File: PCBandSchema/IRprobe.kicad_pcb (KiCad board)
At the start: 2 copper layers, 24 x 16 mm, 21 parts, among them J1 Conn_01x03_Male, Q1 SFH3015FASMALL-FOOTPRINT, U1 ATtiny25-SSU

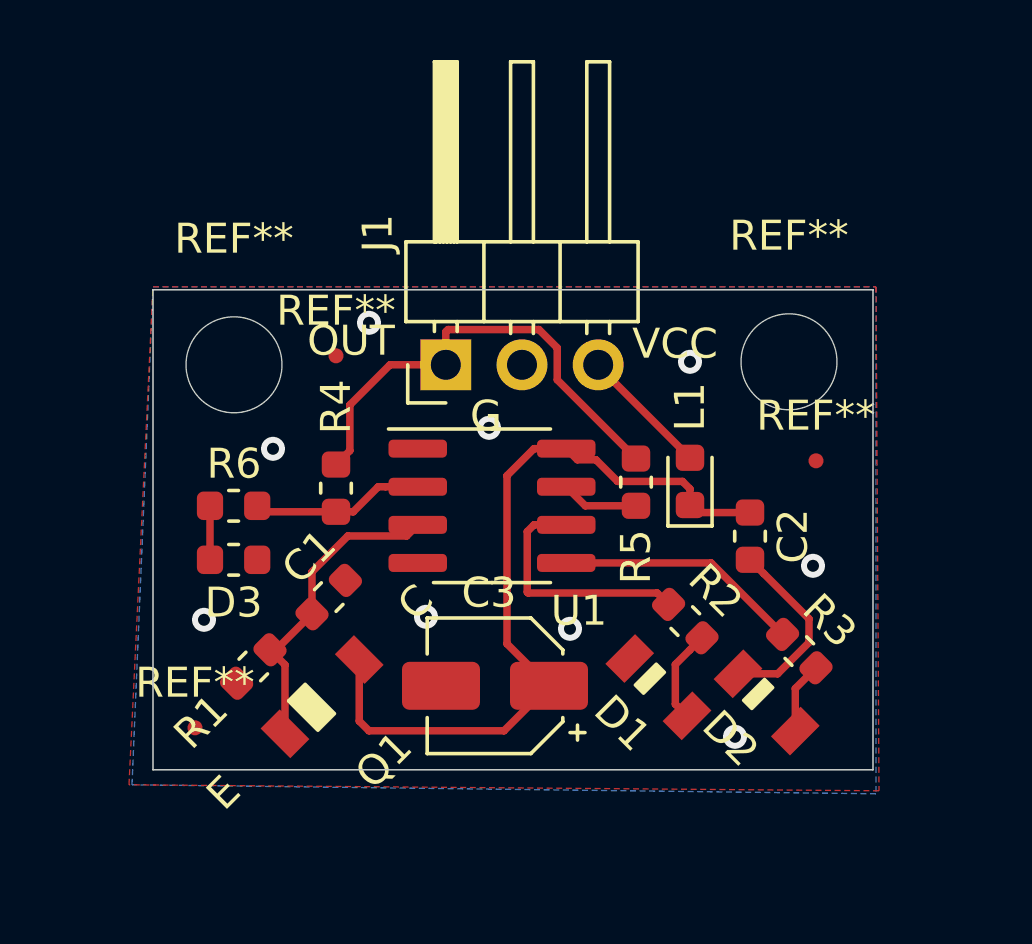
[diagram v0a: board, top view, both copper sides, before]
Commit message: Ver 2 Added ADXL
Second version with same footprint but added ADXL on top of IR probe.
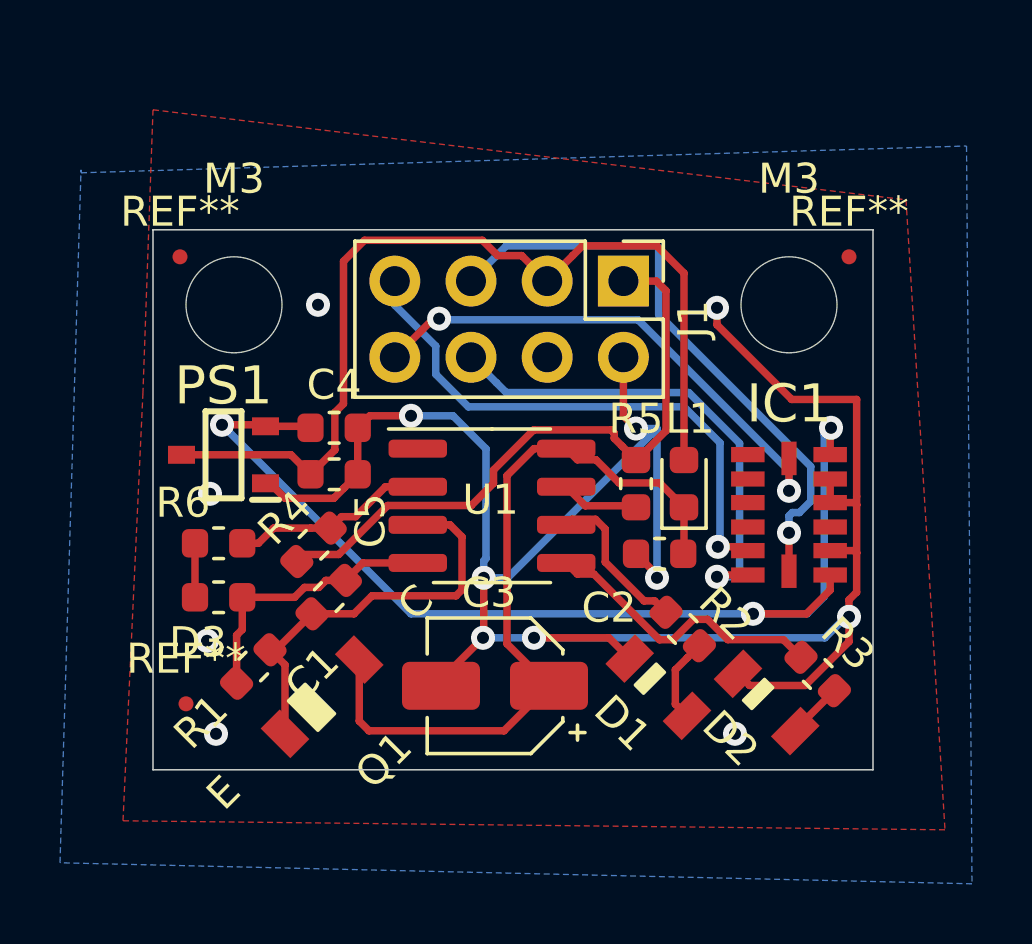
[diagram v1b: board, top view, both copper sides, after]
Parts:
- removed the REF** at (83.0, 62.2)
- removed the REF** at (78.3, 74.6)
- removed the REF** at (99.0, 65.7)
- removed the REF** at (98.1, 62.4)
- added C4: 1u, Capacitor_SMD:C_0603_1608Metric, F.Cu at (82.9, 64.6)
- added C5: 1u, Capacitor_SMD:C_0603_1608Metric, F.Cu at (82.9, 66.2)
- added IC1: ADXL345BCCZ, SamacSys_Parts:LGA14R80P3X6_300X500X100, F.Cu at (98.1, 67.5)
- added M3: MountingHole_3.2mm_M3, MountingHole:MountingHole_3.2mm_M3, F.Cu at (98.1, 60.5)
- added PS1: XC6206P332MR-G, SamacSys_Parts:SOT95P280X130-3N, F.Cu at (79.2, 65.5)
- added REF**: Fiducial_0.5mm_Mask1mm, Fiducial:Fiducial_0.5mm_Mask1mm, F.Cu at (78.0, 73.8)
- added REF**: Fiducial_0.5mm_Mask1mm, Fiducial:Fiducial_0.5mm_Mask1mm, F.Cu at (77.8, 58.9)
- added REF**: Fiducial_0.5mm_Mask1mm, Fiducial:Fiducial_0.5mm_Mask1mm, F.Cu at (100.1, 58.9)
- J1: value Conn_01x03_Male -> Conn_01x08_Male; footprint Connector_PinHeader_2.54mm:PinHeader_1x03_P2.54mm_Horizontal -> Connector_PinHeader_2.54mm:PinHeader_2x04_P2.54mm_Vertical
- moved J1 6.54 mm to (92.6, 59.7), turned to 270 degrees
- moved C2 3.07 mm to (93.8, 68.8), turned to 180 degrees
- moved R4 2.03 mm to (82.2, 68.5), turned to 45 degrees
- moved M3 2.00 mm to (79.6, 60.5)
- moved D3 1.35 mm to (79.1, 70.2)
- moved R6 1.35 mm to (79.1, 68.5)
- moved R3 0.98 mm to (99.1, 72.8)
- moved R2 0.28 mm to (94.6, 71.3)
- moved L1 0.21 mm to (94.6, 66.5)
- moved R5 0.05 mm to (93.0, 66.5)
- renumbered REF** to M3
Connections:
- net Net-(C1-Pad2) renamed GND
- net Net-(J1-Pad1) renamed OUT
- net Net-(J1-Pad3) renamed VCC
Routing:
- net GND: track 6.37 -> 82.5 mm, vias 9 -> 13
- net +3V3: track 0.00 -> 35.9 mm, vias 0 -> 3
- net VCC: track 4.37 -> 31.4 mm
- net SCLK: track 0.00 -> 20.3 mm, vias 0 -> 1
- net MISO: track 0.00 -> 18.6 mm, vias 0 -> 1
- net CS: track 0.00 -> 17.5 mm, vias 0 -> 2
- net MOSI: track 0.00 -> 16.3 mm, vias 0 -> 1
- net OUT: track 15.8 -> 21.5 mm
- net Net-(C1-Pad1): track 10.5 -> 13.6 mm
- net Net-(R2-Pad1): track 8.29 -> 5.33 mm
- net Net-(R3-Pad1): track 8.20 -> 9.69 mm
- net Net-(C2-Pad1): track 26.4 -> 25.4 mm
- net Net-(R4-Pad2): track 5.78 -> 6.63 mm
- net Net-(D2-Pad2): track 2.40 -> 1.89 mm
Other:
- board size 24 x 16 mm -> 24 x 18 mm
- board text removed: "G"
- board text removed: "OUT"
- board text removed: "VCC"
